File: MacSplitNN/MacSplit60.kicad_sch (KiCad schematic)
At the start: 74 parts, among them J1 USB_C_Receptacle_USB2.0, SW1 SW_Push, SW10 SW_Push, SW100 SW_SPST, SW11 SW_Push, SW12 SW_Push, SW13 SW_Push, SW14 SW_Push, SW15 SW_Push, SW16 SW_Push, SW17 SW_Push, SW18 SW_Push, SW19 SW_Push, SW2 SW_Push, SW20 SW_Push, SW21 SW_Push, SW22 SW_Push, SW23 SW_Push, SW24 SW_Push, SW25 SW_Push, SW26 SW_Push, SW27 SW_Push, SW28 SW_Push, SW29 SW_Push, SW3 SW_Push, SW30 SW_Push, SW4 SW_Push, SW5 SW_Push, SW6 SW_Push, SW7 SW_Push, SW8 SW_Push, SW9 SW_Push, U1 Pico, U2 MCP23S17_ML

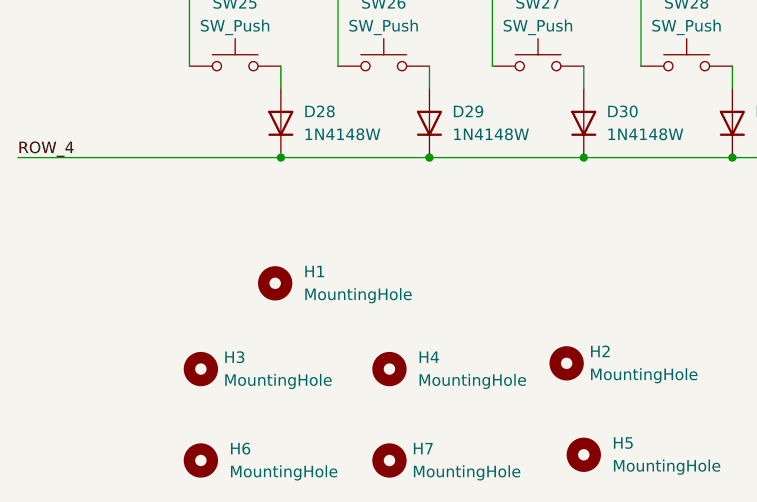
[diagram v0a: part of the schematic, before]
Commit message: Updates switches positions according to MacSplit60 layout
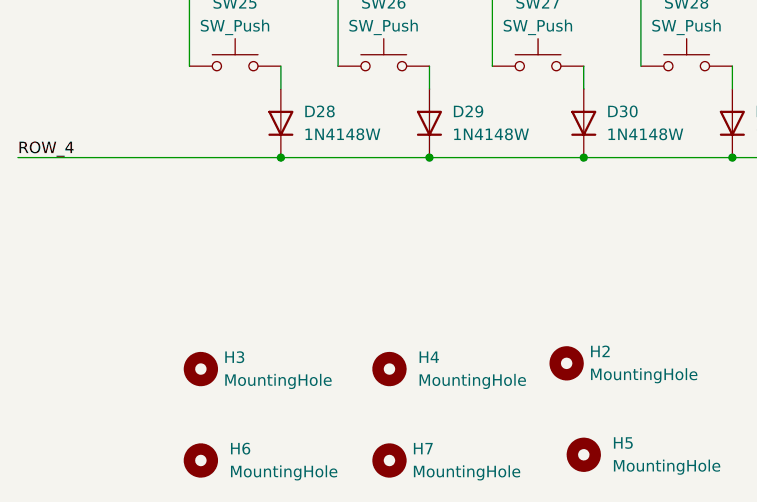
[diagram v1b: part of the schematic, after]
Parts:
- removed H1: MountingHole, MountingHole:MountingHole_2.7mm_M2.5, symbol Mechanical:MountingHole
- SW29, SW30: footprint Switch_Keyboard_Kailh:SW_Kailh_Choc_V1V2_1.00u -> Switch_Keyboard_Kailh:SW_Kailh_Choc_V1V2_1.50u
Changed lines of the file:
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@@
     (property "Reference" "SW29" (id 0) (at 113.665 135.255 0))
     (property "Value" "SW_Push" (id 1) (at 113.665 137.795 0))
-    (property "Footprint" "Switch_Keyboard_Kailh:SW_Kailh_Choc_V1V2_1.00u" (id 2) (at 113.665 137.16 0)
+    (property "Footprint" "Switch_Keyboard_Kailh:SW_Kailh_Choc_V1V2_1.50u" (id 2) (at 113.665 137.16 0)
       (effects (font (size 1.27 1.27)) hide)
     )
@@
     (pin "2")
   )
-  (symbol (lib_id "Mechanical:MountingHole") (at 51.435 166.37 0) (unit 1)
-    (in_bom yes) (on_board yes) (fields_autoplaced)
-    (property "Reference" "H1" (id 0) (at 54.61 165.0999 0)
-      (effects (font (size 1.27 1.27)) (justify left))
-    )
-    (property "Value" "MountingHole" (id 1) (at 54.61 167.6399 0)
-      (effects (font (size 1.27 1.27)) (justify left))
-    )
-    (property "Footprint" "MountingHole:MountingHole_2.7mm_M2.5" (id 2) (at 51.435 166.37 0)
-      (effects (font (size 1.27 1.27)) hide)
-    )
-    (property "Datasheet" "~" (id 3) (at 51.435 166.37 0)
-      (effects (font (size 1.27 1.27)) hide)
-    )
-  )
   (symbol (lib_id "Diode:1N4148W") (at 68.58 60.96 90) (unit 1)
     (in_bom yes) (on_board yes) (fields_autoplaced)
@@
     (property "Reference" "SW30" (id 0) (at 130.175 134.62 0))
     (property "Value" "SW_Push" (id 1) (at 130.175 137.16 0))
-    (property "Footprint" "Switch_Keyboard_Kailh:SW_Kailh_Choc_V1V2_1.00u" (id 2) (at 130.175 137.16 0)
+    (property "Footprint" "Switch_Keyboard_Kailh:SW_Kailh_Choc_V1V2_1.50u" (id 2) (at 130.175 137.16 0)
       (effects (font (size 1.27 1.27)) hide)
     )
@@
       (reference "D33") (unit 1) (value "1N4148W") (footprint "Diode_SMD:D_SOD-123")
     )
-    (path "/c8943267-b756-481f-9147-0e23908c7d5b"
-      (reference "H1") (unit 1) (value "MountingHole") (footprint "MountingHole:MountingHole_2.7mm_M2.5")
-    )
     (path "/e72602a0-4c9b-49c1-aebc-770933c1510b"
       (reference "H2") (unit 1) (value "MountingHole") (footprint "MountingHole:MountingHole_3.2mm_M3")
@@
     )
     (path "/b209455e-4689-40c6-9c5f-6ad42f23df4f"
-      (reference "SW29") (unit 1) (value "SW_Push") (footprint "Switch_Keyboard_Kailh:SW_Kailh_Choc_V1V2_1.00u")
+      (reference "SW29") (unit 1) (value "SW_Push") (footprint "Switch_Keyboard_Kailh:SW_Kailh_Choc_V1V2_1.50u")
     )
     (path "/cf30b61b-518f-4fc0-9759-5e2e77a579bf"
-      (reference "SW30") (unit 1) (value "SW_Push") (footprint "Switch_Keyboard_Kailh:SW_Kailh_Choc_V1V2_1.00u")
+      (reference "SW30") (unit 1) (value "SW_Push") (footprint "Switch_Keyboard_Kailh:SW_Kailh_Choc_V1V2_1.50u")
     )
     (path "/d341b761-c583-465c-b8e1-18cf1d826c04"

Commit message: Equalises and checks switches spacing, diodes on both layers
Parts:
- D1, D10, D11, D12, D13, D14, D15, D16, D17, D18, D19, D2, D20, D21, D22, D23, D24, D25, D26, D27, D28, D29, D3, D30, D31, D32, D33, D4, D5, D6: footprint Diode_SMD:D_SOD-123 -> Diode_SMD:D_SOD-323_Hand_Split_Keyboard

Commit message: Changes USB-C footprint to circular hole and pad
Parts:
- J1: footprint Connector_USB:USB_C_Receptacle_GCT_USB4085 -> Connector_USB:USB_C_Receptacle_GCT_USB4085_Circular
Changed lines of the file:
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@@
     (property "Reference" "J1" (id 0) (at 167.005 91.44 0))
     (property "Value" "USB_C_Receptacle_USB2.0" (id 1) (at 167.005 93.98 0))
-    (property "Footprint" "Connector_USB:USB_C_Receptacle_GCT_USB4085" (id 2) (at 170.815 114.3 0)
+    (property "Footprint" "Connector_USB:USB_C_Receptacle_GCT_USB4085_Circular" (id 2) (at 170.815 114.3 0)
       (effects (font (size 1.27 1.27)) hide)
     )
@@
     )
     (path "/d137f386-2ca0-4a22-9eae-481a6c0fd279"
-      (reference "J1") (unit 1) (value "USB_C_Receptacle_USB2.0") (footprint "Connector_USB:USB_C_Receptacle_GCT_USB4085")
+      (reference "J1") (unit 1) (value "USB_C_Receptacle_USB2.0") (footprint "Connector_USB:USB_C_Receptacle_GCT_USB4085_Circular")
     )
     (path "/16c030dd-9a18-4f80-b59a-3f4922a29869"

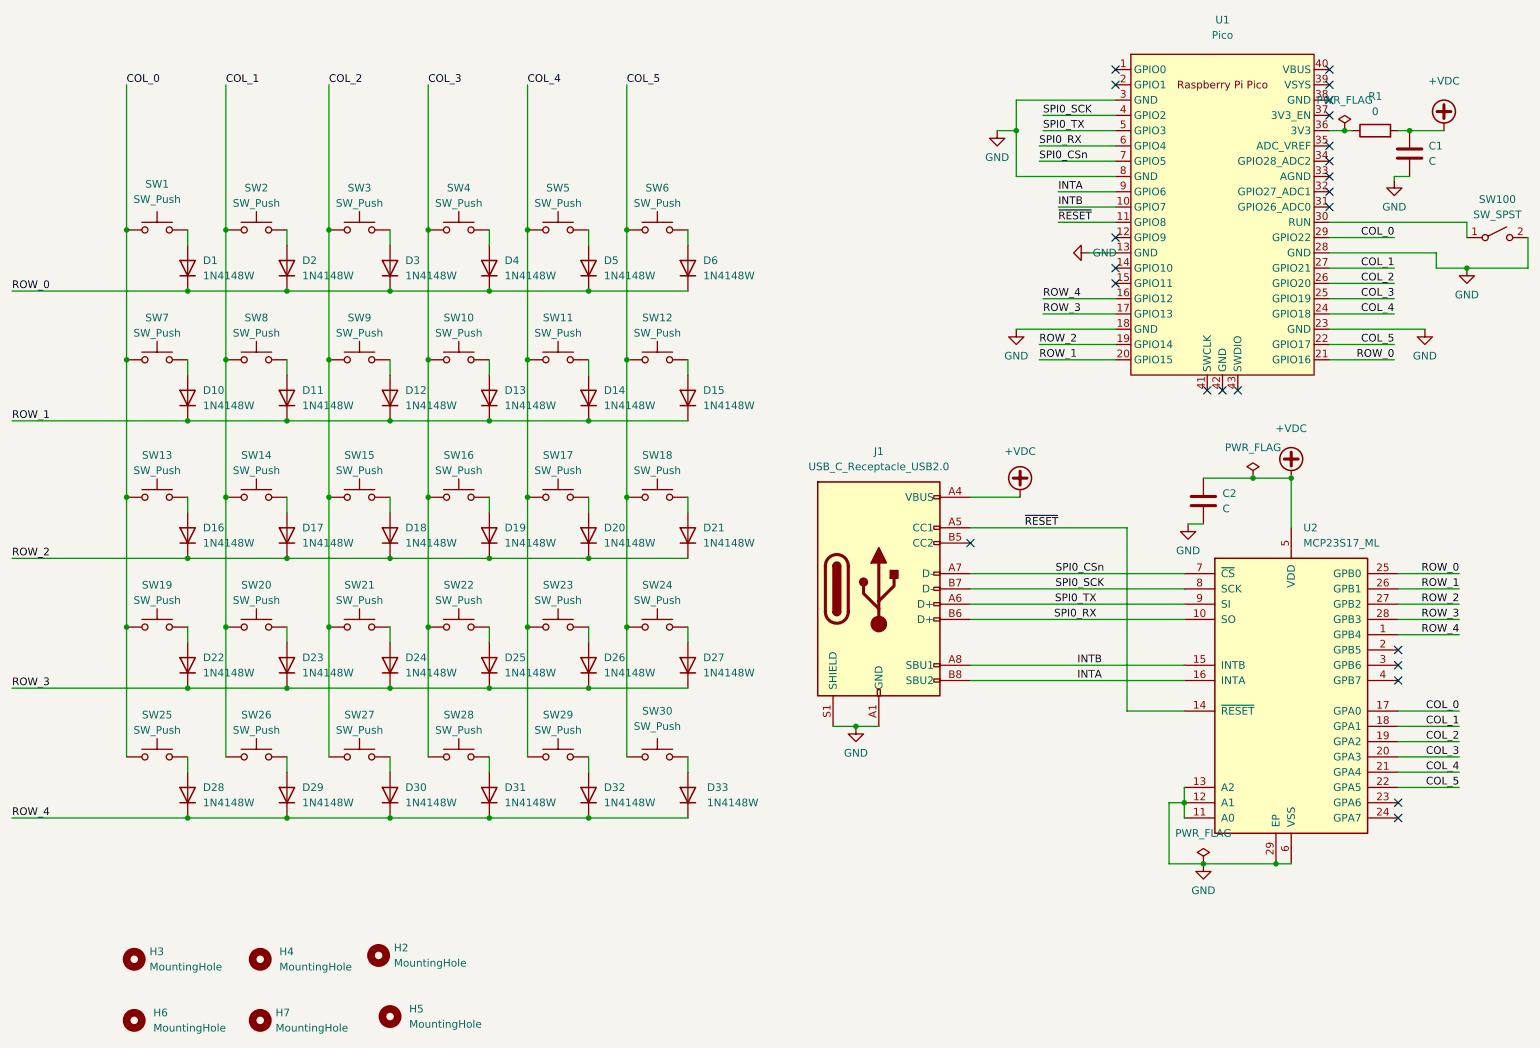
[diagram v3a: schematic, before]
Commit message: Modify switches footprints, TRRS board to board
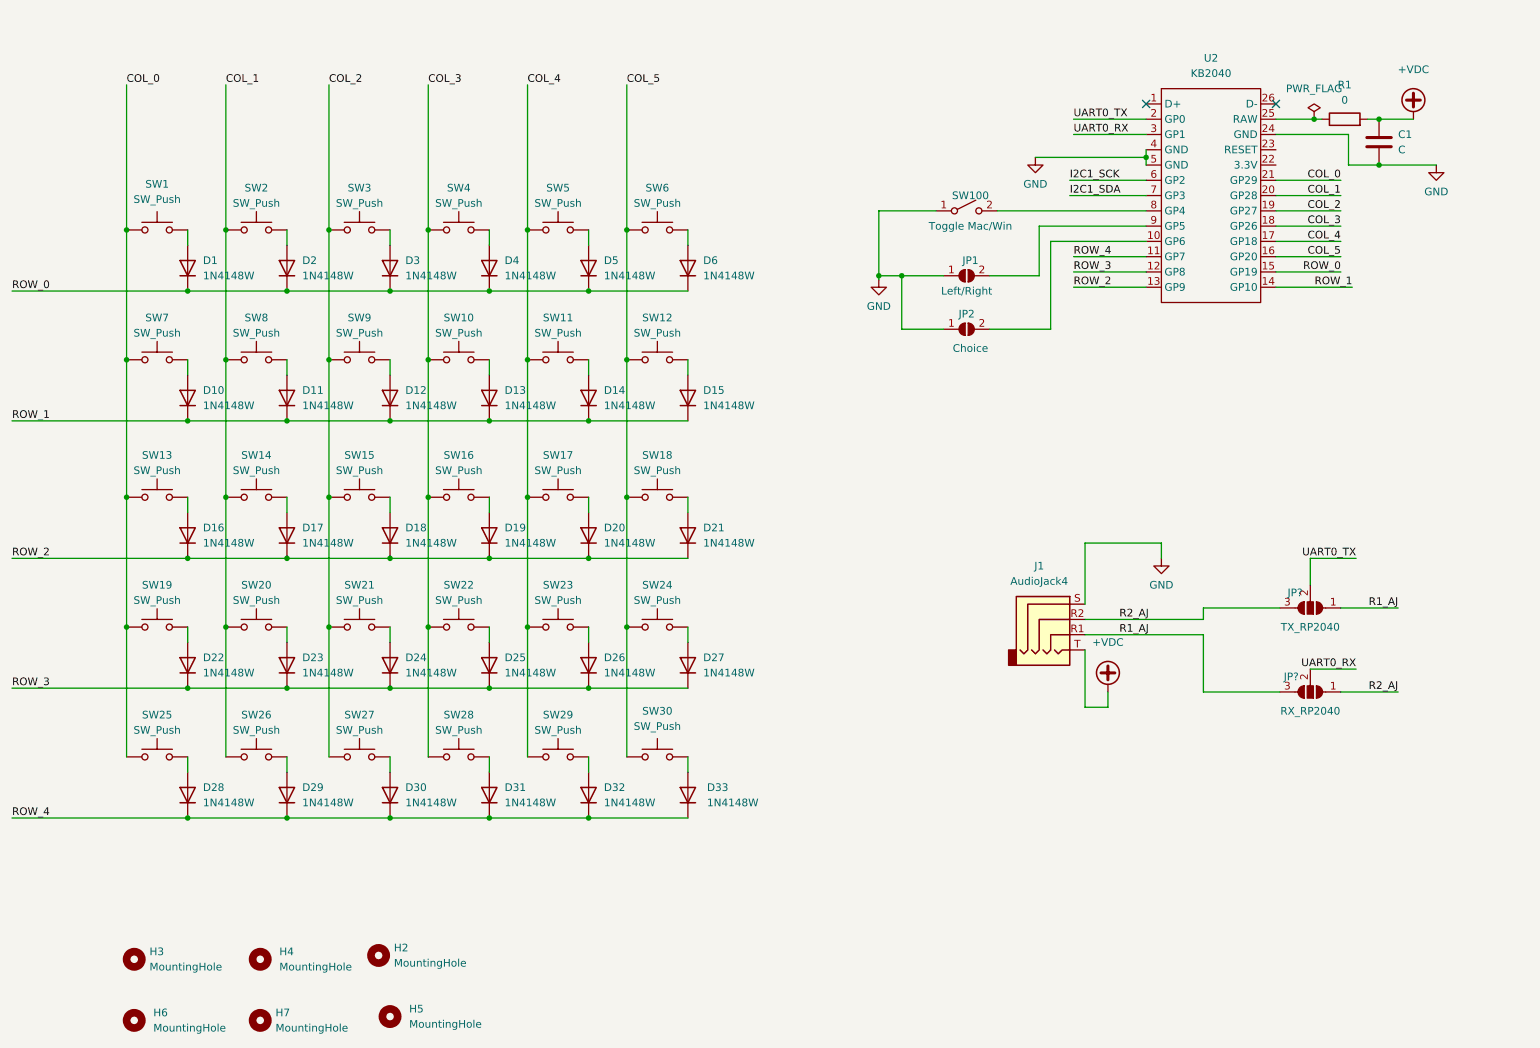
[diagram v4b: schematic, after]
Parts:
- removed C2: C, Capacitor_SMD:C_0603_1608Metric, symbol Device:C
- removed J1: USB_C_Receptacle_USB2.0, Connector_USB:USB_C_Receptacle_GCT_USB4085_Circular, symbol Connector:USB_C_Receptacle_USB2.0
- removed U1: Pico, MCU_RaspberryPi_and_Boards:RPi_Pico_SMD_TH, symbol MCU_RaspberryPi_and_Boards:Pico
- removed U2: MCP23S17_ML, Package_DFN_QFN:QFN-28-1EP_6x6mm_P0.65mm_EP4.25x4.25mm, symbol Interface_Expansion:MCP23S17_ML
- added J1: AudioJack4, Connector_Audio:Jack_3.5mm_CUI_SJ2-3574A-SMT_Horizontal, symbol Connector:AudioJack4
- added JP1: Left/Right, symbol Jumper:SolderJumper_2_Open
- added JP2: Choice, Jumper:SolderJumper-2_P1.3mm_Open_TrianglePad1.0x1.5mm, symbol Jumper:SolderJumper_2_Open
- added JP?: RX_RP2040, symbol Jumper:SolderJumper_3_Open
- added JP?: TX_RP2040, symbol Jumper:SolderJumper_3_Open
- added U2: KB2040, KB2040:Adafruit_KB2040, symbol KB2040:KB2040
- SW1, SW10, SW11, SW12, SW14, SW15, SW16, SW17, SW18, SW2, SW20, SW21, SW22, SW23, SW24, SW25, SW26, SW3, SW4, SW5, SW6, SW7, SW8, SW9: footprint Switch_Keyboard_Kailh:SW_Kailh_Choc_V1V2_1.00u -> Button_Switch_Keyboard:SW_Cherry_MX_1.00u_Plate
- SW100: value SW_SPST -> Toggle Mac/Win; footprint Button_Switch_SMD:SW_SPST_CK_RS282G05A3 -> (none)
- SW13, SW19: footprint Switch_Keyboard_Kailh:SW_Kailh_Choc_V1V2_2.00u -> Button_Switch_Keyboard:SW_Cherry_MX_2.00u_Plate
- SW27, SW28, SW29, SW30: footprint Switch_Keyboard_Kailh:SW_Kailh_Choc_V1V2_1.50u -> Button_Switch_Keyboard:SW_Cherry_MX_1.50u_Plate
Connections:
- net +VDC: now also J1.T
- net COL_0: now also U2.21 (GP29)
- net COL_1: now also U2.20 (GP28)
- net COL_2: now also U2.19 (GP27)
- net COL_3: now also U2.18 (GP26)
- net COL_4: now also U2.17 (GP18)
- net COL_5: now also U2.16 (GP20)
- net GND: now also SW100.1 (A), J1.S, JP1.1 (A), JP2.1 (A), U2.24 (GND), U2.4 (GND), U2.5 (GND); no longer SW100.2 (B)
- net ROW_0: now also U2.15 (GP19)
- net ROW_1: now also U2.14 (GP10)
- net ROW_2: now also U2.13 (GP9)
- net ROW_3: now also U2.12 (GP8)
- net ROW_4: now also U2.11 (GP7)
- net at R1.1: now also U2.25 (RAW)
- new net: JP2.2 (B), U2.10 (GP6)
- new net: SW100.2 (B), U2.8 (GP4)
- new net: JP1.2 (B), U2.9 (GP5)
- new net I2C1_SCK: U2.6 (GP2)
- new net I2C1_SDA: U2.7 (GP3)
- new net R1_AJ: J1.R1, JP?.1 (A), JP?.3 (B)
- new net R2_AJ: J1.R2, JP?.1 (A), JP?.3 (B)
- new net UART0_RX: JP?.2 (C), U2.3 (GP1)
- new net UART0_TX: JP?.2 (C), U2.2 (GP0)
- no-connect marks 23 -> 2
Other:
- moved on the sheet: C1, R1

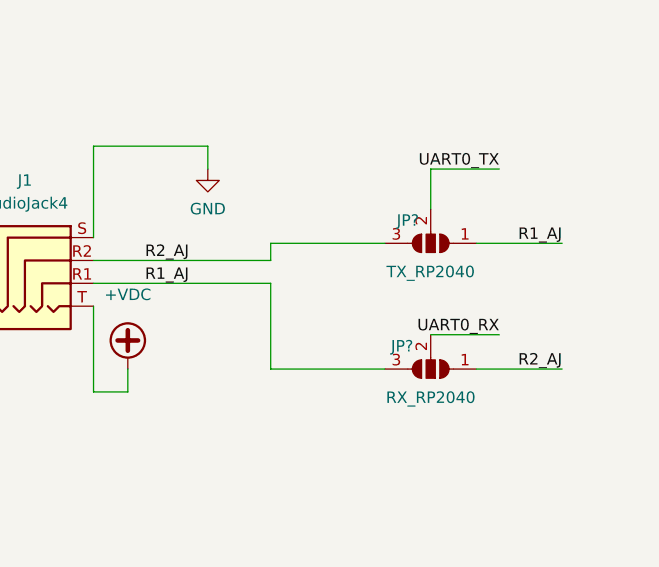
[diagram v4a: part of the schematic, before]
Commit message: remove all vias, tracks
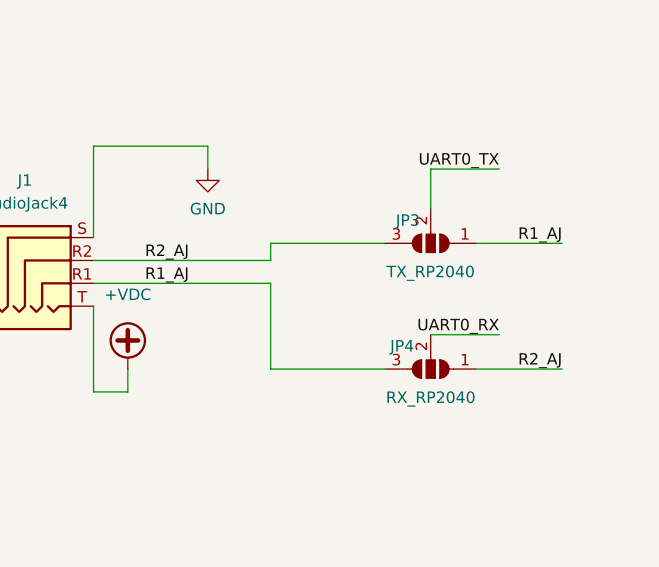
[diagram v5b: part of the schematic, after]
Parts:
- JP1: footprint (none) -> Jumper:SolderJumper-2_P1.3mm_Open_TrianglePad1.0x1.5mm
- JP3, JP4: renamed from JP?; footprint (none) -> Jumper:SolderJumper-3_P1.3mm_Open_Pad1.0x1.5mm_NumberLabels
- SW100: footprint (none) -> Button_Switch_SMD:SW_SPST_CK_RS282G05A3
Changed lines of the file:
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@@
   (symbol (lib_id "power:GND") (at 213.995 109.22 0) (unit 1)
     (in_bom yes) (on_board yes) (fields_autoplaced)
-    (property "Reference" "#PWR?" (id 0) (at 213.995 115.57 0)
+    (property "Reference" "#PWR0102" (id 0) (at 213.995 115.57 0)
       (effects (font (size 1.27 1.27)) hide)
     )
@@
   (symbol (lib_id "Jumper:SolderJumper_3_Open") (at 238.76 131.445 180) (unit 1)
     (in_bom yes) (on_board yes)
-    (property "Reference" "JP?" (id 0) (at 235.585 128.905 0))
+    (property "Reference" "JP4" (id 0) (at 235.585 128.905 0))
     (property "Value" "RX_RP2040" (id 1) (at 238.76 134.62 0))
-    (property "Footprint" "" (id 2) (at 238.76 131.445 0)
+    (property "Footprint" "Jumper:SolderJumper-3_P1.3mm_Open_Pad1.0x1.5mm_NumberLabels" (id 2) (at 238.76 131.445 0)
       (effects (font (size 1.27 1.27)) hide)
     )
@@
     (property "Reference" "SW100" (id 0) (at 182.245 48.895 0))
     (property "Value" "Toggle Mac/Win" (id 1) (at 182.245 53.975 0))
-    (property "Footprint" "" (id 2) (at 181.61 51.435 0)
+    (property "Footprint" "Button_Switch_SMD:SW_SPST_CK_RS282G05A3" (id 2) (at 181.61 51.435 0)
       (effects (font (size 1.27 1.27)) hide)
     )
@@
     (property "Reference" "JP1" (id 0) (at 182.245 59.69 0))
     (property "Value" "Left/Right" (id 1) (at 181.61 64.77 0))
-    (property "Footprint" "" (id 2) (at 181.61 62.23 0)
+    (property "Footprint" "Jumper:SolderJumper-2_P1.3mm_Open_TrianglePad1.0x1.5mm" (id 2) (at 181.61 62.23 0)
       (effects (font (size 1.27 1.27)) hide)
     )
@@
   (symbol (lib_id "power:+VDC") (at 205.105 131.445 0) (unit 1)
     (in_bom yes) (on_board yes) (fields_autoplaced)
-    (property "Reference" "#PWR?" (id 0) (at 205.105 133.985 0)
+    (property "Reference" "#PWR0103" (id 0) (at 205.105 133.985 0)
       (effects (font (size 1.27 1.27)) hide)
     )
@@
   (symbol (lib_id "Jumper:SolderJumper_3_Open") (at 238.76 117.475 180) (unit 1)
     (in_bom yes) (on_board yes)
-    (property "Reference" "JP?" (id 0) (at 236.22 114.935 0))
+    (property "Reference" "JP3" (id 0) (at 236.22 114.935 0))
     (property "Value" "TX_RP2040" (id 1) (at 238.76 120.65 0))
-    (property "Footprint" "" (id 2) (at 238.76 117.475 0)
+    (property "Footprint" "Jumper:SolderJumper-3_P1.3mm_Open_Pad1.0x1.5mm_NumberLabels" (id 2) (at 238.76 117.475 0)
       (effects (font (size 1.27 1.27)) hide)
     )
@@
     )
     (path "/3ecd4da5-781f-4878-bc75-8c025a2cbd29"
-      (reference "#PWR?") (unit 1) (value "GND") (footprint "")
+      (reference "#PWR0102") (unit 1) (value "GND") (footprint "")
     )
     (path "/b0a1e65d-3a26-4633-b3bf-3ffda2bfe67e"
-      (reference "#PWR?") (unit 1) (value "+VDC") (footprint "")
+      (reference "#PWR0103") (unit 1) (value "+VDC") (footprint "")
     )
     (path "/1503565f-b461-4b6f-a205-df2f3236546f"
@@
       (reference "JP2") (unit 1) (value "Choice") (footprint "Jumper:SolderJumper-2_P1.3mm_Open_TrianglePad1.0x1.5mm")
     )
+    (path "/ba7492e4-52d5-4172-83a9-89726ecbce05"
+      (reference "JP3") (unit 1) (value "TX_RP2040") (footprint "Jumper:SolderJumper-3_P1.3mm_Open_Pad1.0x1.5mm_NumberLabels")
+    )
     (path "/625bff50-6d7b-4a08-9061-45f53bfbc727"
-      (reference "JP?") (unit 1) (value "RX_RP2040") (footprint "")
-    )
-    (path "/ba7492e4-52d5-4172-83a9-89726ecbce05"
-      (reference "JP?") (unit 1) (value "TX_RP2040") (footprint "")
+      (reference "JP4") (unit 1) (value "RX_RP2040") (footprint "Jumper:SolderJumper-3_P1.3mm_Open_Pad1.0x1.5mm_NumberLabels")
     )
     (path "/16c030dd-9a18-4f80-b59a-3f4922a29869"
@@
     )
     (path "/79cf6d6f-d083-4216-a814-79d3190fefb5"
-      (reference "SW100") (unit 1) (value "Toggle Mac/Win") (footprint "")
+      (reference "SW100") (unit 1) (value "Toggle Mac/Win") (footprint "Button_Switch_SMD:SW_SPST_CK_RS282G05A3")
     )
     (path "/3d0fec0a-0fd9-457c-964a-54992763e3c6"

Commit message: Update footprint, start repositioning keys
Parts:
- SW1, SW10, SW11, SW12, SW14, SW15, SW16, SW17, SW18, SW2, SW20, SW21, SW22, SW23, SW24, SW25, SW26, SW3, SW4, SW5, SW6, SW7, SW8, SW9: footprint Button_Switch_Keyboard:SW_Cherry_MX_1.00u_Plate -> Lily58-footprint:MX_PG1350-DoubleSide_Keycap_18mm_1.00u
- SW13, SW19: footprint Button_Switch_Keyboard:SW_Cherry_MX_2.00u_Plate -> Lily58-footprint:MX_PG1350-DoubleSide_Keycap_28mm_1.50u
- SW27, SW28, SW29, SW30: footprint Button_Switch_Keyboard:SW_Cherry_MX_1.50u_Plate -> Lily58-footprint:MX_PG1350-DoubleSide_Keycap_28mm_1.50u
